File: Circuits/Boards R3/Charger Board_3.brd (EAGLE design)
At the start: 97.2 x 69.8 mm, 129 parts, among them CON1 ISP(2X3), CON13 HEADER_4X1, CON14 HEADER_3X1, CON15 HEADER_3X1, CON16 HEADER_4X1, CON17 HEADER_3X1, CON19 HEADER_4X1, CON2 SCREWTERMINAL_1X2, CON20 HEADER_4X1, CON21 HEADER_4X1, CON22 HEADER_4X1, CON23 HEADER_4X1, CON24 HEADER_4X1, CON25 HEADER_4X1, CON26 HEADER_4X1, CON27 HEADER_4X1, CON28 HEADER_4X1, CON3 HEADER_4X1, CON4 HEADER_4X1, CON5 HEADER_4X1, CON6 HEADER_4X1, CON7 HEADER_4X1, CON8 HEADER_4X1, T1 IRLML6244TR, T2 IRLML6244TR, T3 SI4421DY, T4 IRLML6244TR, T5 IRLML6244TR, T6 IRLML6244TR, T7 IRLML6244TR, U1 ATMEGA324P, U2 ACS711, U3 JOYSTICKPTH, U4 MX25L25735E, U5 ATMEGA1281, U6 CD74HC154M96

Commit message: ready to route
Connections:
- new net LED6: R32.2
- new net LED7: R33.2
- net BUZZER: now also U5.P$1
- net LED4: now also R34.2, U5.P$7; no longer R35.2
- net LED5: now also R35.2; no longer R33.2
- net MISO: no longer R32.2
- net MOSI: no longer R34.2
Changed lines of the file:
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@@
 <wire x1="20.13" y1="35.751" x2="26.9755" y2="42.5965" width="0.254" layer="1"/>
 <wire x1="26.9755" y1="42.5965" x2="26.9755" y2="52.1335" width="0.254" layer="1"/>
+<contactref element="U5" pad="P$1"/>
+<wire x1="20.13" y1="31.15" x2="-59.185" y2="-11.399" width="0" layer="19" extent="1-1"/>
 </signal>
 <signal name="+5V">
@@
 <wire x1="15.367" y1="29.21" x2="12.7" y2="29.21" width="0.254" layer="16"/>
 <contactref element="U5" pad="P$12"/>
-<contactref element="R34" pad="2"/>
-<wire x1="-54.749" y1="-0.381" x2="-59.185" y2="-20.199" width="0" layer="19" extent="1-1"/>
-<wire x1="4.217" y1="37.084" x2="-54.749" y2="-0.381" width="0" layer="19" extent="1-1"/>
+<wire x1="7.747" y1="32.639" x2="-59.185" y2="-20.199" width="0" layer="19" extent="1-1"/>
 </signal>
 <signal name="MISO">
@@
 <wire x1="10.414" y1="31.75" x2="10.16" y2="31.75" width="0.254" layer="1"/>
 <contactref element="U5" pad="P$13"/>
-<contactref element="R32" pad="2"/>
-<wire x1="-48.653" y1="-0.381" x2="-59.185" y2="-20.999" width="0" layer="19" extent="1-1"/>
-<wire x1="10.16" y1="31.75" x2="-48.653" y2="-0.381" width="0" layer="19" extent="1-1"/>
+<wire x1="10.16" y1="31.75" x2="-59.185" y2="-20.999" width="0" layer="19" extent="1-1"/>
 </signal>
 <signal name="SCK">
@@
 </signal>
 <signal name="LED5">
-<contactref element="R33" pad="2"/>
+<contactref element="R35" pad="2"/>
 </signal>
 <signal name="LED4">
-<contactref element="R35" pad="2"/>
+<contactref element="U5" pad="P$7"/>
+<contactref element="R34" pad="2"/>
+<wire x1="-54.749" y1="-0.381" x2="-59.185" y2="-16.199" width="0" layer="19" extent="1-1"/>
 </signal>
 <signal name="N$46">
@@
 <contactref element="TST1" pad="P$1"/>
 </signal>
+<signal name="LED6">
+<contactref element="R32" pad="2"/>
+</signal>
+<signal name="LED7">
+<contactref element="R33" pad="2"/>
+</signal>
 </signals>

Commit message: both boards are routed
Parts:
- removed U1: ATMEGA324P, DigitalIC:TQFP44
- R17, R18, R19, R2, R20, R3, R37, R38, R39, R4, R40, R41, R42, R5, R6, R9: value 300 -> 1k
- moved TST2 223.9 mm to (50.1, 22.1)
- moved C25 221.7 mm to (22.5, 41.3), turned to 180 degrees
- moved TST1 217.1 mm to (39.9, 23.1)
- moved U6 207.5 mm to (25.1, 32.6), turned to 270 degrees
- moved R43 206.8 mm to (22.3, 23.8), turned to 180 degrees
- moved R37 187.9 mm to (14.4, 21.0), turned to 180 degrees
- moved R38 184.4 mm to (14.4, 18.4), turned to 180 degrees
- moved R39 180.9 mm to (14.4, 15.9), turned to 180 degrees
- moved R40 177.5 mm to (14.4, 13.3), turned to 180 degrees
- moved R41 174.0 mm to (14.4, 10.8), turned to 180 degrees
- moved R42 170.6 mm to (14.4, 8.26), turned to 180 degrees
- moved CON7 168.9 mm to (5.84, 10.8)
- moved CON5 165.6 mm to (5.84, 15.9)
- moved CON3 162.3 mm to (5.84, 21.0)
- moved CON8 162.2 mm to (5.84, 8.26)
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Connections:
- net A0: now also U5.P$16
- net A1: now also U5.P$17
- net A2: now also U5.P$18
- net A3: now also U5.P$19
- net BLUE: now also CON16.2; no longer CON16.1
- net BUTTON: no longer U1.34
- net BUZZER: no longer U1.44
- net CHARGER: now also U5.P$44; no longer U1.40
- net CS: now also U5.P$9; no longer U1.30
- net CURRENTSENSE: now also U5.P$59; no longer U1.37
- net DEBUG1: now also U5.P$43
- net DEBUG2: now also U5.P$33
- net GREEN: now also CON16.1; no longer CON16.2
- net HOLD: now also U5.P$15; no longer U1.31
- net HORIZONTAL: now also U5.P$61; no longer U1.35
- net LED1: now also U5.P$39; no longer U1.41
- net LED2: now also U5.P$38; no longer U1.42
- net LED3: now also U5.P$37; no longer U1.43
- net LED5: now also U5.P$34
- net LED6: now also U5.P$35
- net LED7: now also U5.P$49
- net TRANSMITLEDS: now also U5.P$10; no longer U1.33
- net VERTICAL: now also U5.P$60; no longer U1.36
- net WP: now also U5.P$14; no longer U1.32
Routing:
- net +3V: track 174.7 -> 278.7 mm, vias 5 -> 6
- net CRX: track 0.00 -> 89.2 mm, vias 0 -> 2
- net CHARGE+: track 7.62 -> 92.1 mm, vias 0 -> 2
- net GND: track 40.5 -> 123.8 mm, vias 5 -> 12
- net LED6: track 0.00 -> 55.1 mm, vias 0 -> 2
- net LED5: track 0.00 -> 52.1 mm, vias 0 -> 2
- net CHARGER: track 50.6 -> 4.92 mm, vias 2 -> 0
- net CTX16: track 0.00 -> 43.0 mm, vias 0 -> 1
- net LED4: track 0.00 -> 42.6 mm, vias 0 -> 2
- net CTX15: track 0.00 -> 39.8 mm, vias 0 -> 1
- net CTX14: track 0.00 -> 36.5 mm, vias 0 -> 1
- net BUZZER: track 23.8 -> 58.4 mm, vias 0 -> 2
- net CTX13: track 0.00 -> 33.3 mm, vias 0 -> 1
- net CTX12: track 0.00 -> 30.1 mm, vias 0 -> 1
- net N$55: track 0.00 -> 30.1 mm, vias 0 -> 2
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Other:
- board text added: "3/19/14"
- board text removed: "12/10/12"
- board text removed: "UART 2"

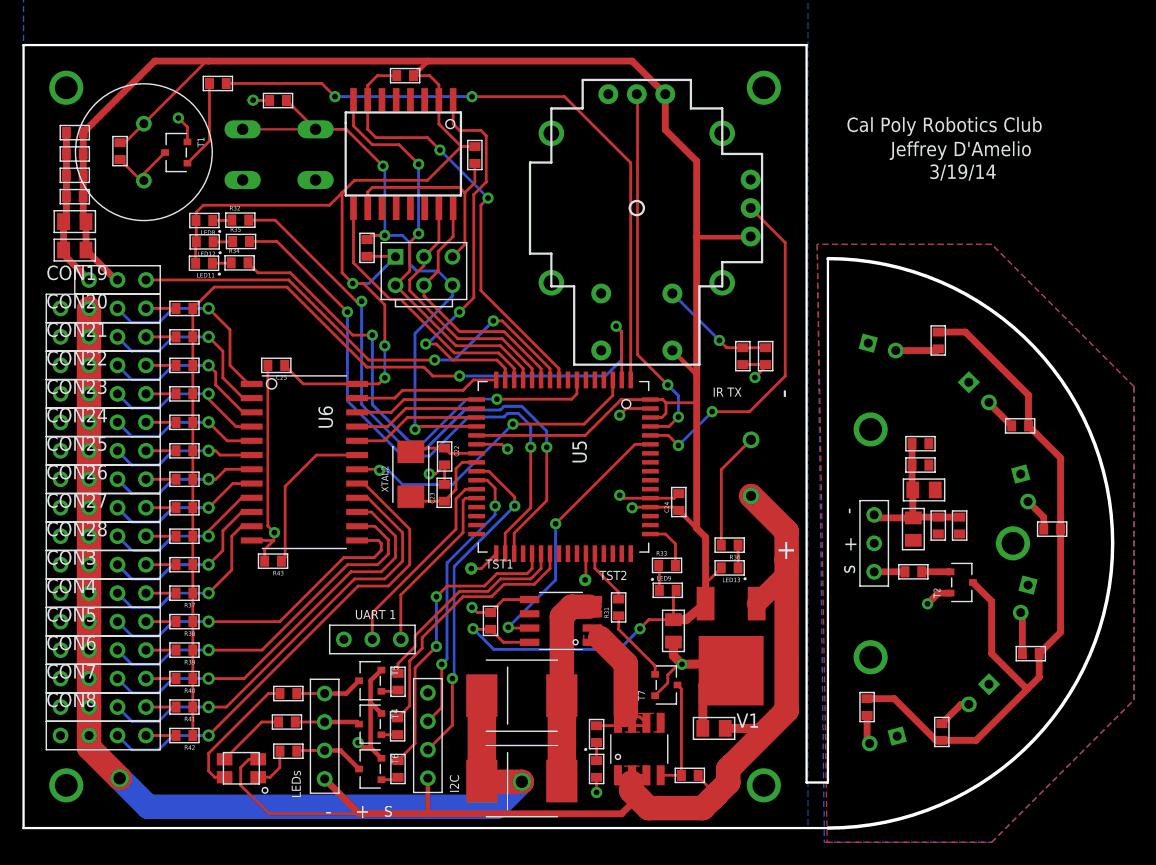
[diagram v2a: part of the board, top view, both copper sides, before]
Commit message: updated part outlines in tplace layer
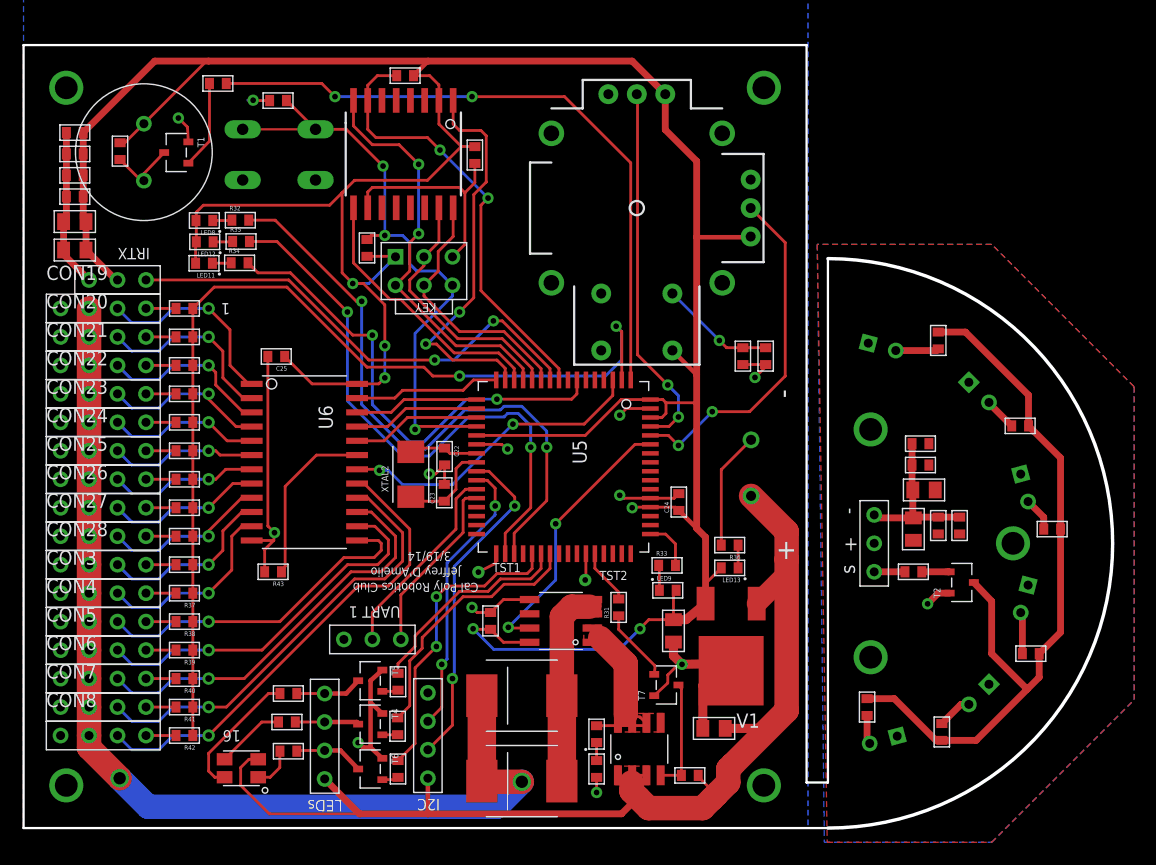
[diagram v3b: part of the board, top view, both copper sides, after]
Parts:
- moved R43 0.95 mm to (22.3, 22.9)
- moved C25 0.79 mm to (22.5, 42.1)
- moved TST1 0.71 mm to (40.6, 22.8)
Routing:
- net GND: track 123.8 -> 125.7 mm
- net N$57: track 14.4 -> 15.3 mm
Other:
- board text added: "1"
- board text added: "16"
- board text added: "IRTX"
- board text added: "KEY"
- board text removed: "IR TX"

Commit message: Gerbers generated and zipped for boards and stencils
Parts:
- moved C12 0.64 mm to (82.2, 27.0)
- moved C2 0.64 mm to (84.1, 27.0)
- moved C6 0.64 mm to (80.0, 26.7)
- moved C8 0.64 mm to (81.0, 30.2)
- moved C7 0.63 mm to (80.6, 34.3)
- moved C9 0.63 mm to (80.6, 32.4)
- moved S1 0.35 mm to (22.6, 59.8), flipped to the top
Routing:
- net RESET: track 54.5 -> 57.9 mm
- net N$5: track 16.8 -> 17.4 mm
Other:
- board text added: "RXI"
- board text added: "TXO"
- board text added: "UART"
- board text removed: "UART 1"

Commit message: BOMS and boards updated with a few slight value changes to reflect component availability
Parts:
- LED10: value red -> RED
- R1: value 310 -> 220
- R21, R22: value 200 -> 70
- R27: value 470 -> 1k
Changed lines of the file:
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@@
 <element name="LED6" library="Passive" package="5MM_LED_RA" value="IR" x="89.281" y="30.353" smashed="yes" rot="R285"/>
 <element name="C6" library="Passive" package="0805" value="10uf" x="80.01" y="26.67" smashed="yes" rot="R90"/>
-<element name="LED10" library="Passive" package="LED0603" value="red" x="51.1175" y="8.382" smashed="yes" rot="R90"/>
-<element name="R27" library="Passive" package="0603" value="470" x="51.1175" y="5.2705" smashed="yes" rot="R90"/>
+<element name="LED10" library="Passive" package="LED0603" value="RED" x="51.1175" y="8.382" smashed="yes" rot="R90"/>
+<element name="R27" library="Passive" package="0603" value="1k" x="51.1175" y="5.2705" smashed="yes" rot="R90"/>
 <element name="R28" library="Passive" package="0603" value="1k" x="17.3355" y="66.421" smashed="yes" rot="R180"/>
 <element name="U2" library="PowerIC" package="8SOIC" value="ACS711" x="47.9425" y="18.4785" smashed="yes" rot="R90"/>
@@
 <element name="CON2" library="Mechanical" package="SCREWTERMINAL_1X2" value="SCREWTERMINAL_1X2" x="64.897" y="32.131" smashed="yes" rot="R90"/>
 <element name="LED1" library="Passive" package="PLCC4" value="SMD_RGB" x="19.431" y="5.334" smashed="yes" rot="R180"/>
-<element name="R1" library="Passive" package="0603" value="310" x="23.622" y="6.858" smashed="yes" rot="R180"/>
-<element name="R21" library="Passive" package="0603" value="200" x="23.495" y="9.4615" smashed="yes" rot="R180"/>
-<element name="R22" library="Passive" package="0603" value="200" x="23.622" y="12.0015" smashed="yes" rot="R180"/>
+<element name="R1" library="Passive" package="0603" value="220" x="23.622" y="6.858" smashed="yes" rot="R180"/>
+<element name="R21" library="Passive" package="0603" value="70" x="23.495" y="9.4615" smashed="yes" rot="R180"/>
+<element name="R22" library="Passive" package="0603" value="70" x="23.622" y="12.0015" smashed="yes" rot="R180"/>
 <element name="C2" library="Passive" package="0603" value=".1uf" x="84.1375" y="26.9875" smashed="yes" rot="R90"/>
 <element name="C7" library="Passive" package="0603" value=".1uf" x="80.645" y="34.29" smashed="yes" rot="R180"/>
